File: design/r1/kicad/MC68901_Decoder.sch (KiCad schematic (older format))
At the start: 15 parts, among them IC2 ATF16V8QL-15PU, IC3 7493N, IC4 MC68901P, Q1 1.8432MHz

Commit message: Initial cleanup
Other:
- note added: "1"
- note added: "Copyright ©2019-2020 Ross Bamford and Contributors.\nOpen Source Hardware licenced under CERN Open Hardware Licence. \nSee https://github.com/roscopeco/rosco_m68k/blob/master/LICENCE.hardware.txt\nOSHWA UK000006 (https://certification.oshwa.org/uk000006.html)\n"
- note added: "MC68901 & DECODER"
- note removed: "& DECODER"
- note removed: "MC68901"
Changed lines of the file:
@@
-$EndComp
-$Comp
-L rosco_m68k-eagle-import:A3L-LOC #FRAME2
-U 1 1 70888A22
-P 1100 10300
-AR Path="/70888A22" Ref="#FRAME2"  Part="1"
-AR Path="/5E53B630/70888A22" Ref="#FRAME2"  Part="1"
-F 0 "#FRAME2" H 1100 10300 50  0001 C CNN
-F 1 "BOOT line generator" H 1100 10300 50  0001 C CNN
-F 2 "" H 1100 10300 50  0001 C CNN
-F 3 "" H 1100 10300 50  0001 C CNN
-	1    1100 10300
-	1    0    0    -1
 $EndComp
 $Comp
@@
 	1    0    0    -1
 $EndComp
-Text Notes 12900 9700 0    170  ~ 0
-MC68901
-Text Notes 12700 10000 0    170  ~ 0
-& DECODER
 NoConn ~ 11200 5500
 NoConn ~ 11200 5600
@@
 	14300 1100 2700 1100
 Wire Bus Line
+	2700 800  2700 1100
+Connection ~ 2700 1100
+Text Notes 18650 9800 0    59   ~ 0
+Copyright ©2019-2020 Ross Bamford and Contributors.\nOpen Source Hardware licenced under CERN Open Hardware Licence. \nSee https://github.com/roscopeco/rosco_m68k/blob/master/LICENCE.hardware.txt\nOSHWA UK000006 (https://certification.oshwa.org/uk000006.html)\n
+Text Notes 22200 10500 0    59   ~ 0
+1
+Text Notes 18950 10350 0    59   ~ 0
+MC68901 & DECODER
+Wire Bus Line
 	8200 3700 8200 4400
 Wire Bus Line
@@
 	3300 6800 3300 8000
 Wire Bus Line
-	2700 800  2700 1100
+	2700 1100 2700 9300
 Wire Bus Line
 	6500 6900 6500 8300
 Wire Bus Line
 	13000 5100 13000 5900
-Connection ~ 2700 1100
-Wire Bus Line
-	2700 1100 2700 9300
 $EndSCHEMATC

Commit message: Cleanup first pass
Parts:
- Q1: value 1.8432MHz -> 3.6864MHz
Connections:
- net labels added: BOOT, IACK, IODTACK, MFPDS, RW
- net labels removed: /BOOT, /IACK, /IODTACK, /MFPDS, A0, A10, A11, A12, A13, A14, A15, A16, A24, A6, A7, A8, A9, CONTROL:AS,BERR,BG,BGACK,BR,CLK,DTACK,EVENRAMSEL,EVENROMSEL,EXPSEL,FC0,FC1,FC2,IOSEL,IPL0,IPL1,IPL2,LDS,ODDRAMSEL,ODDROMSEL,RESET,R/W,UDS, R/W
- wire segments 120 -> 117
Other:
- note added: "MC68901"
- moved on the sheet: C10, C11, C12, C13, C14, IC3B, IC4A, IC4B, JP1, LED1, LED2, Q1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

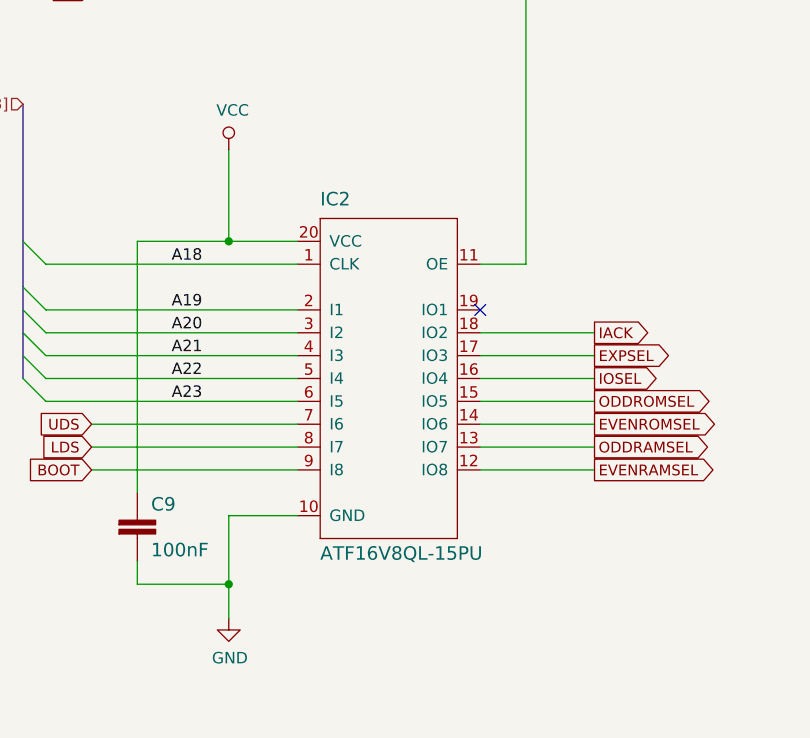
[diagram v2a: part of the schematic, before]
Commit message: Fixing migrated symbols
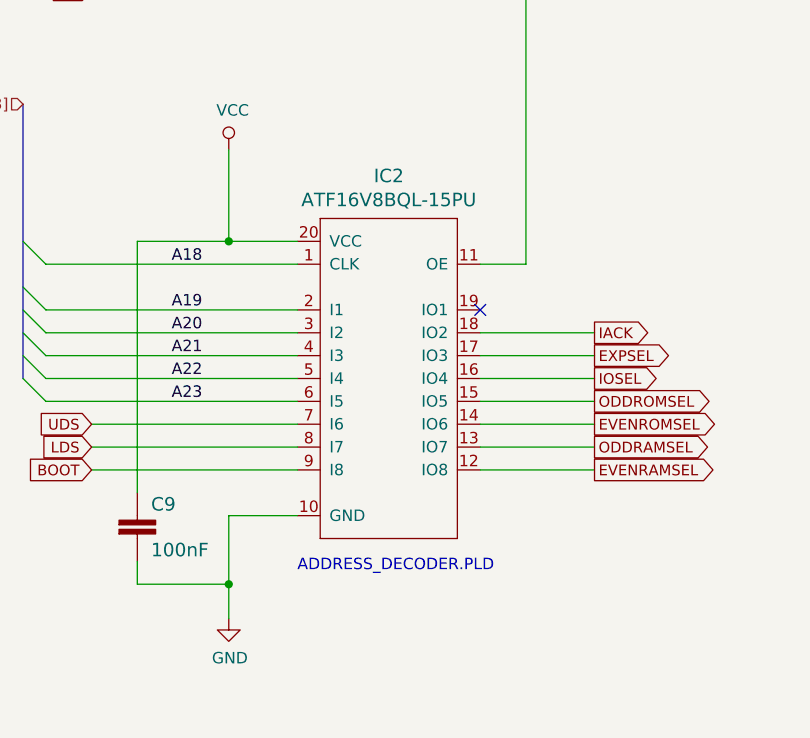
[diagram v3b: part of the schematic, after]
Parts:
- IC2: value ATF16V8QL-15PU -> ATF16V8BQL-15PU; footprint rosco_m68k:DIL20 -> (none); MPN ATF16V8QL-15PU -> (none); PROG ADDRESS_DECODER.PLD -> (none)
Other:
- note added: "ADDRESS_DECODER.PLD"
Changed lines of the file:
@@
 	14250 4700 14350 4600
-$Comp
-L rosco_m68k-eagle-import:ATF16V8BP3 IC2
-U 1 1 D1EC01D6
-P 4900 8000
-AR Path="/D1EC01D6" Ref="IC2"  Part="1"
-AR Path="/5E53B630/D1EC01D6" Ref="IC2"  Part="1"
-F 0 "IC2" H 4600 8750 59  0000 L BNN
-F 1 "ATF16V8QL-15PU" H 4600 7200 59  0000 L BNN
-F 2 "rosco_m68k:DIL20" H 4900 8000 50  0001 C CNN
-F 3 "" H 4900 8000 50  0001 C CNN
-F 4 "ATF16V8QL-15PU" H 4900 8000 59  0001 L BNN "MPN"
-F 5 "ADDRESS_DECODER.PLD" H 4600 7100 59  0001 L BNN "PROG"
-	1    4900 8000
-	1    0    0    -1
-$EndComp
 $Comp
 L rosco_m68k-eagle-import:MC68901P IC4
@@
 Wire Bus Line
 	14350 4500 14350 5300
+$Comp
+L rosco_m68k-eagle-import:ATF16V8BP3 IC2
+U 1 1 5FE9651B
+P 4900 8000
+F 0 "IC2" H 4900 8886 59  0000 C CNN
+F 1 "ATF16V8BQL-15PU" H 4900 8781 59  0000 C CNN
+F 2 "" H 4900 8000 50  0001 C CNN
+F 3 "" H 4900 8000 50  0001 C CNN
+	1    4900 8000
+	1    0    0    -1
+$EndComp
+Text Notes 4500 8850 0    50   ~ 0
+ADDRESS_DECODER.PLD
 $EndSCHEMATC

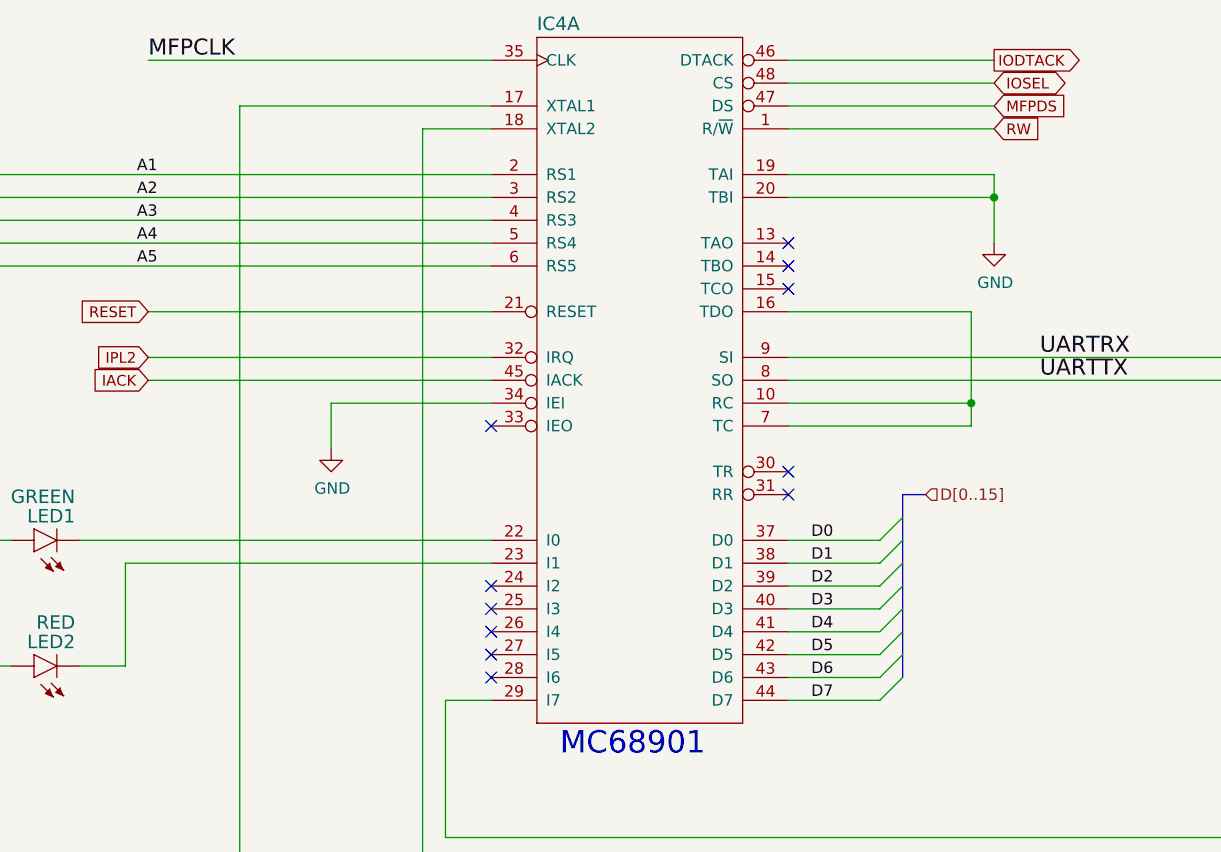
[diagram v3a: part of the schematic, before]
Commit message: GPIO, Legacy Peripheral and Panel support
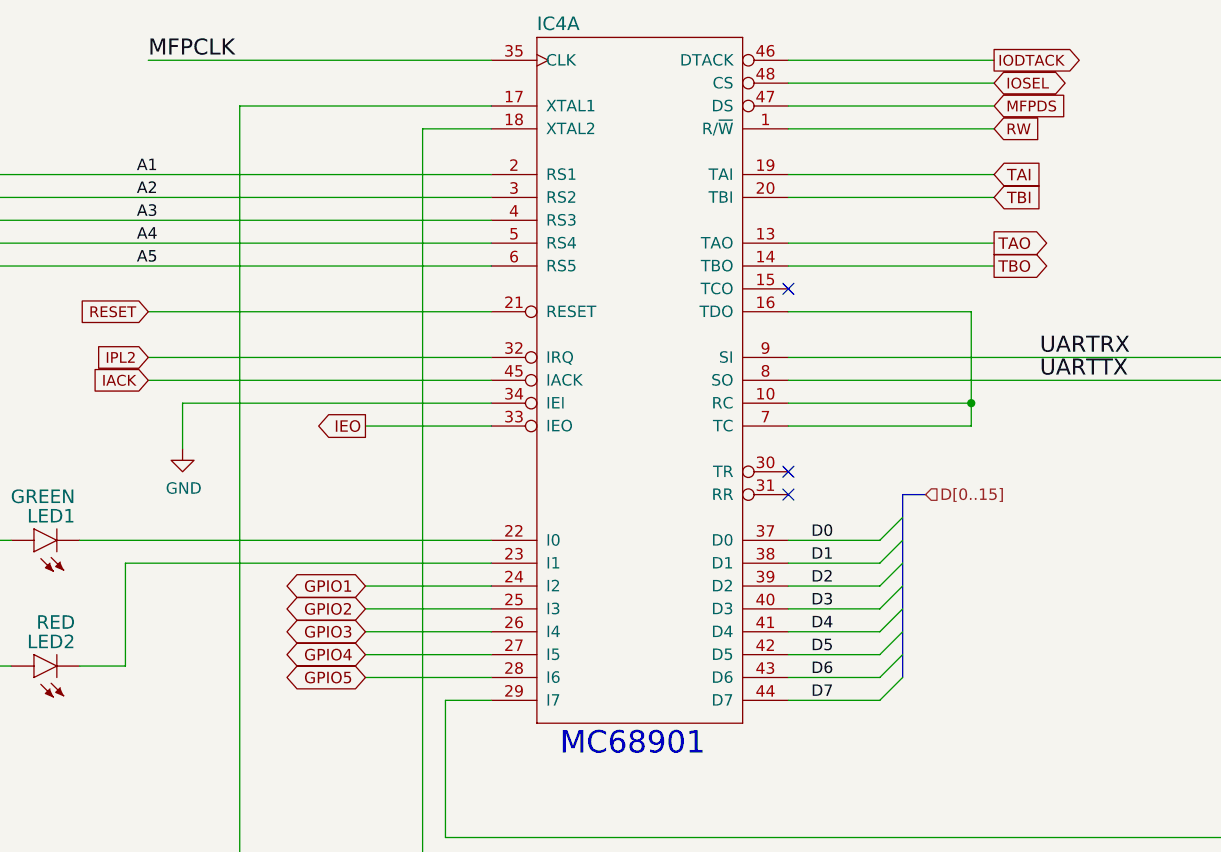
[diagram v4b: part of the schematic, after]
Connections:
- net GND: no longer IC4.19 (TAI), IC4.20 (TBI)
- net TAO: now reaches IC4.13 (TAO)
- net TBO: now reaches IC4.14 (TBO)
- net GPIO1: now reaches IC4.24 (I2)
- net GPIO2: now reaches IC4.25 (I3)
- net GPIO3: now reaches IC4.26 (I4)
- net GPIO4: now reaches IC4.27 (I5)
- net GPIO5: now reaches IC4.28 (I6)
- net IEO: now reaches IC4.33 (IEO)
- new net TAI: IC4.19 (TAI)
- new net TBI: IC4.20 (TBI)
- no-connect marks 15 -> 7
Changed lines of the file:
@@
 	3800 8900 4200 8900
 Wire Wire Line
-	12550 4100 11850 4100
-Wire Wire Line
-	11850 4100 11850 4300
-Wire Wire Line
-	13850 3100 14750 3100
-Wire Wire Line
-	14750 3100 14750 3200
-Wire Wire Line
-	13850 3200 14750 3200
-Connection ~ 14750 3200
+	12550 4100 11200 4100
+Wire Wire Line
+	11200 4100 11200 4300
 Wire Wire Line
 	21800 8050 21800 7650
@@
 	1    0    0    -1
 $EndComp
-NoConn ~ 12550 4900
-NoConn ~ 12550 5000
-NoConn ~ 12550 5100
-NoConn ~ 12550 5200
-NoConn ~ 12550 5300
 NoConn ~ 5300 7700
 NoConn ~ 5500 2600
@@
 NoConn ~ 13850 4400
 NoConn ~ 13850 4500
-NoConn ~ 13850 3400
-NoConn ~ 13850 3500
-NoConn ~ 13850 3600
-NoConn ~ 12550 4200
 Text Label 13950 4700 0    50   ~ 0
 D0
@@
 Wire Wire Line
 	13850 2900 14750 2900
-$Comp
-L power:GND #PWR0112
-U 1 1 5F9ED783
-P 14750 3400
-F 0 "#PWR0112" H 14750 3150 50  0001 C CNN
-F 1 "GND" H 14755 3227 50  0000 C CNN
-F 2 "" H 14750 3400 50  0001 C CNN
-F 3 "" H 14750 3400 50  0001 C CNN
-	1    14750 3400
-	1    0    0    -1
-$EndComp
-Wire Wire Line
-	14750 3200 14750 3400
 Wire Wire Line
 	11050 3700 12550 3700
@@
 L power:GND #PWR0124
 U 1 1 5FBAA792
-P 11850 4300
-F 0 "#PWR0124" H 11850 4050 50  0001 C CNN
-F 1 "GND" H 11855 4127 50  0000 C CNN
-F 2 "" H 11850 4300 50  0001 C CNN
-F 3 "" H 11850 4300 50  0001 C CNN
-	1    11850 4300
-	1    0    0    -1
-$EndComp
-Wire Bus Line
-	10150 2900 10150 3400
-Wire Bus Line
-	3300 6800 3300 8000
-Wire Bus Line
-	14350 4500 14350 5300
+P 11200 4300
+F 0 "#PWR0124" H 11200 4050 50  0001 C CNN
+F 1 "GND" H 11205 4127 50  0000 C CNN
+F 2 "" H 11200 4300 50  0001 C CNN
+F 3 "" H 11200 4300 50  0001 C CNN
+	1    11200 4300
+	1    0    0    -1
+$EndComp
 $Comp
 L rosco_m68k-eagle-import:ATF16V8BP3 IC2
@@
 Text Notes 4500 8850 0    50   ~ 0
 ADDRESS_DECODER.PLD
+Wire Wire Line
+	12550 4900 12000 4900
+Wire Wire Line
+	12550 5000 12000 5000
+Wire Wire Line
+	12550 5100 12000 5100
+Wire Wire Line
+	12550 5200 12000 5200
+Wire Wire Line
+	12550 5300 12000 5300
+Text GLabel 12000 4900 0    50   BiDi ~ 0
+GPIO1
+Text GLabel 12000 5000 0    50   BiDi ~ 0
+GPIO2
+Text GLabel 12000 5100 0    50   BiDi ~ 0
+GPIO3
+Text GLabel 12000 5200 0    50   BiDi ~ 0
+GPIO4
+Text GLabel 12000 5300 0    50   BiDi ~ 0
+GPIO5
+Wire Wire Line
+	13850 3100 14750 3100
+Wire Wire Line
+	13850 3200 14750 3200
+Wire Wire Line
+	13850 3400 14750 3400
+Wire Wire Line
+	13850 3500 14750 3500
+Text GLabel 14750 3100 2    50   Input ~ 0
+TAI
+Text GLabel 14750 3200 2    50   Input ~ 0
+TBI
+Text GLabel 14750 3400 2    50   Output ~ 0
+TAO
+Text GLabel 14750 3500 2    50   Output ~ 0
+TBO
+Wire Wire Line
+	12550 4200 12000 4200
+Text GLabel 12000 4200 0    50   Output ~ 0
+IEO
+NoConn ~ 13850 3600
+Wire Bus Line
+	10150 2900 10150 3400
+Wire Bus Line
+	3300 6800 3300 8000
+Wire Bus Line
+	14350 4500 14350 5300
 $EndSCHEMATC

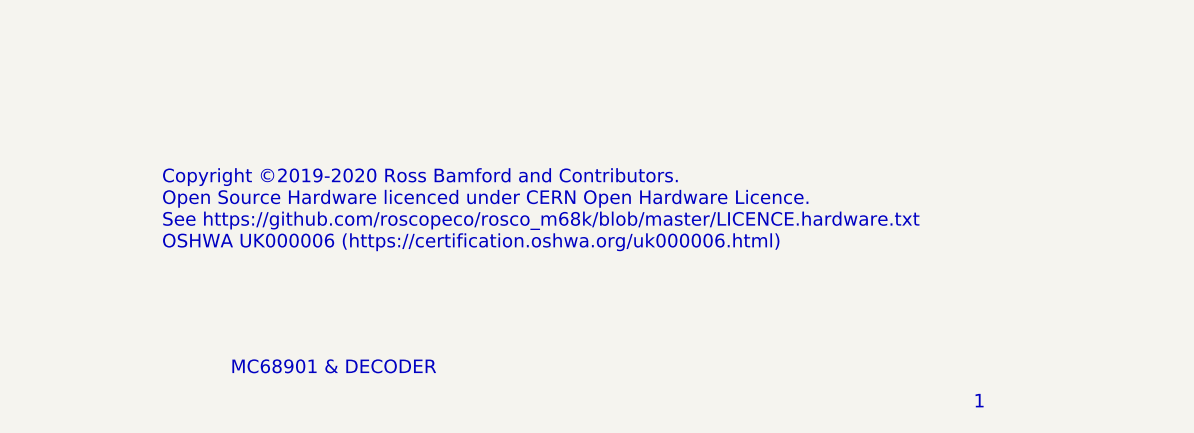
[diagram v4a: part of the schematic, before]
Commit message: Fix #18 and apply suggestions from #17
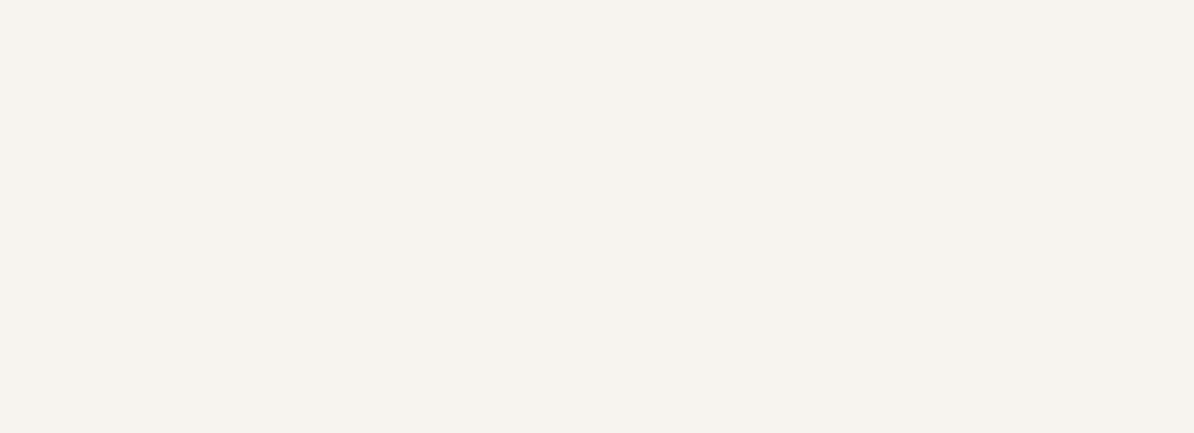
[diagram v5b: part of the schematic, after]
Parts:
- IC2: footprint (none) -> rosco_m68k:DIL20
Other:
- note removed: "1"
- note removed: "Copyright ©2019-2020 Ross Bamford and Contributors.\nOpen Source Hardware licenced under CERN Open Hardware Licence. \nSee https://github.com/roscopeco/rosco_m68k/blob/master/LICENCE.hardware.txt\nOSHWA UK000006 (https://certification.oshwa.org/uk000006.html)\n"
- note removed: "MC68901 & DECODER"
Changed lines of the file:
@@
 encoding utf-8
 Sheet 3 6
-Title ""
+Title "MC68901 & DECODER"
 Date "2020-02-25"
-Rev ""
+Rev "1"
 Comp ""
-Comment1 ""
-Comment2 ""
-Comment3 ""
-Comment4 ""
+Comment1 "OSHWA UK000006 (https://certification.oshwa.org/uk000006.html)"
+Comment2 "See https://github.com/roscopeco/rosco_m68k/blob/master/LICENCE.hardware.txt"
+Comment3 "Open Source Hardware licenced under CERN Open Hardware Licence"
+Comment4 "Copyright 2019-2020 Ross Bamford and Contributors"
 $EndDescr
 Wire Wire Line
@@
 Text Label 11000 3100 0    50   ~ 0
 A1
-Text Notes 18650 9800 0    59   ~ 0
-Copyright ©2019-2020 Ross Bamford and Contributors.\nOpen Source Hardware licenced under CERN Open Hardware Licence. \nSee https://github.com/roscopeco/rosco_m68k/blob/master/LICENCE.hardware.txt\nOSHWA UK000006 (https://certification.oshwa.org/uk000006.html)\n
-Text Notes 22200 10500 0    59   ~ 0
-1
-Text Notes 18950 10350 0    59   ~ 0
-MC68901 & DECODER
 Text Notes 12850 5650 0    98   ~ 0
 MC68901
@@
 F 0 "IC2" H 4900 8886 59  0000 C CNN
 F 1 "ATF16V8BQL-15PU" H 4900 8781 59  0000 C CNN
-F 2 "" H 4900 8000 50  0001 C CNN
+F 2 "rosco_m68k:DIL20" H 4900 8000 50  0001 C CNN
 F 3 "" H 4900 8000 50  0001 C CNN
 	1    4900 8000

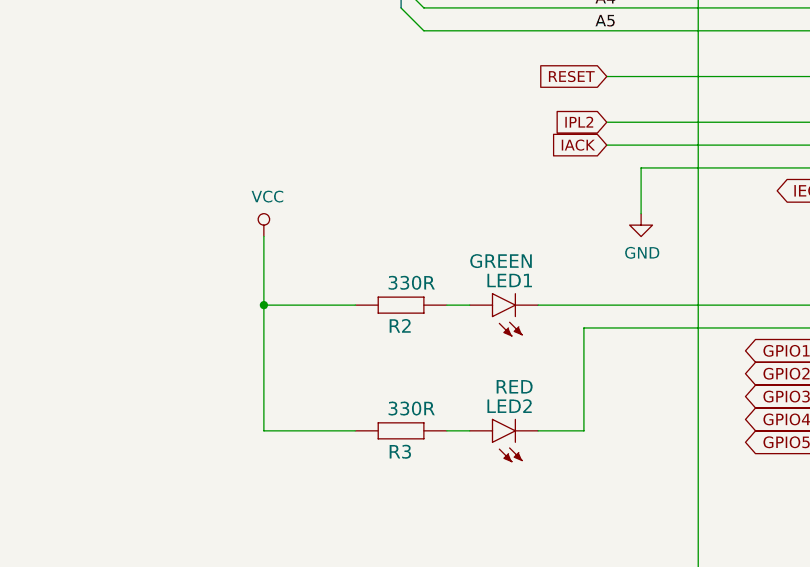
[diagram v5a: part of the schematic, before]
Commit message: Fix limiting resistors on R2 and R15
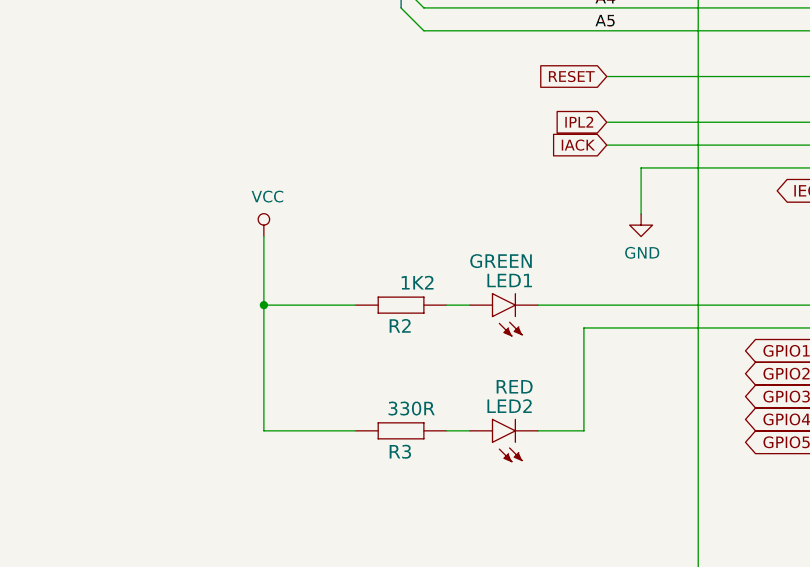
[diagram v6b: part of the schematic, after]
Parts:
- R2: value 330R -> 1K2
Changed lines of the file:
@@
 AR Path="/5E53B630/FD9490FA" Ref="R2"  Part="1"
 F 0 "R2" H 10100 4759 59  0000 L BNN
-F 1 "330R" H 10000 4570 59  0000 L BNN
+F 1 "1K2" H 10000 4570 59  0000 L BNN
 F 2 "rosco_m68k:0207_10" H 10150 4700 50  0001 C CNN
 F 3 "" H 10150 4700 50  0001 C CNN
